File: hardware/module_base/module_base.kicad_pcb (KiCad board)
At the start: 2 copper layers, 100 x 100 mm, 38 parts, among them J1 RJ45_Shielded, J2 Conn_01x24_Female, J3 Conn_01x32_Female, Q1 Q_NMOS_GSD, Q2 Q_NMOS_GSD, Q3 Q_NMOS_GSD, Q4 Q_NMOS_GSD, Q5 Q_NMOS_GSD, Q6 Q_NMOS_GSD, U1 WAVGAT_CAN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

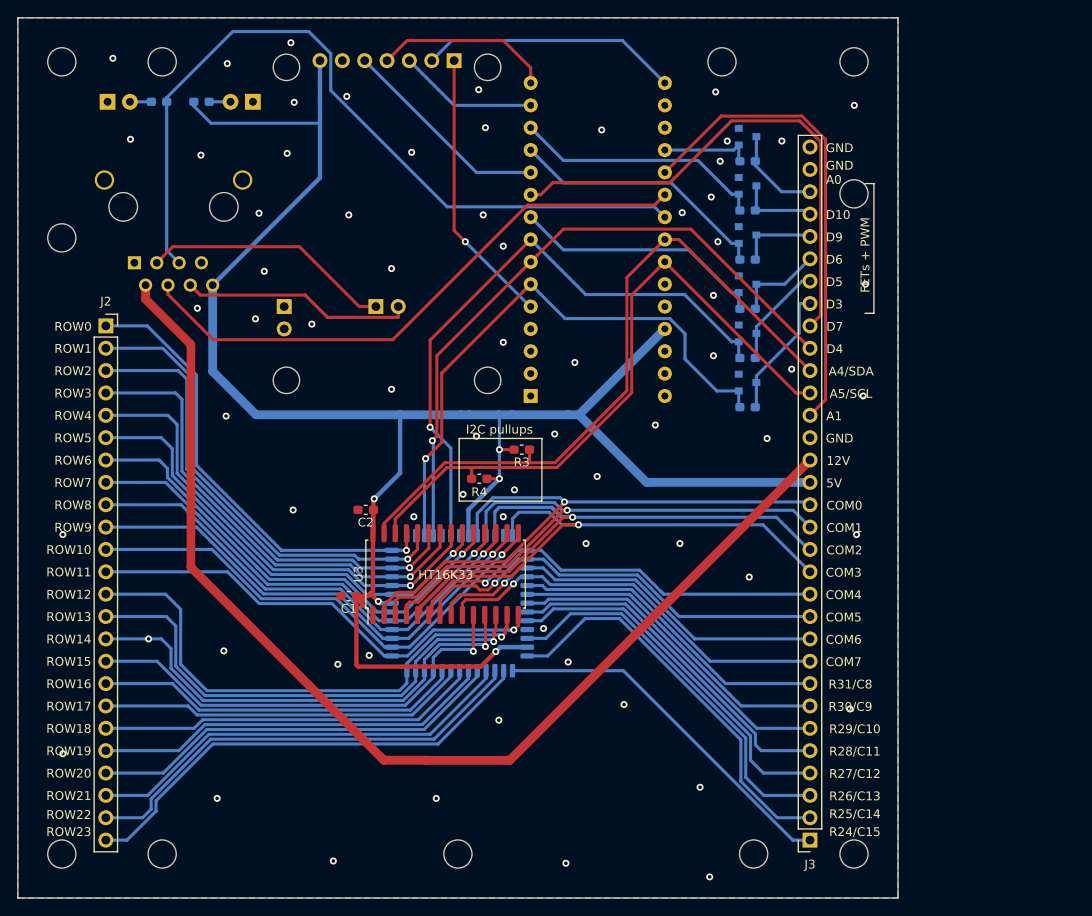
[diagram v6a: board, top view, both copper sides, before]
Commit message: ModuleBase PCB: expose Arduino pins + SPI + more GND/5V
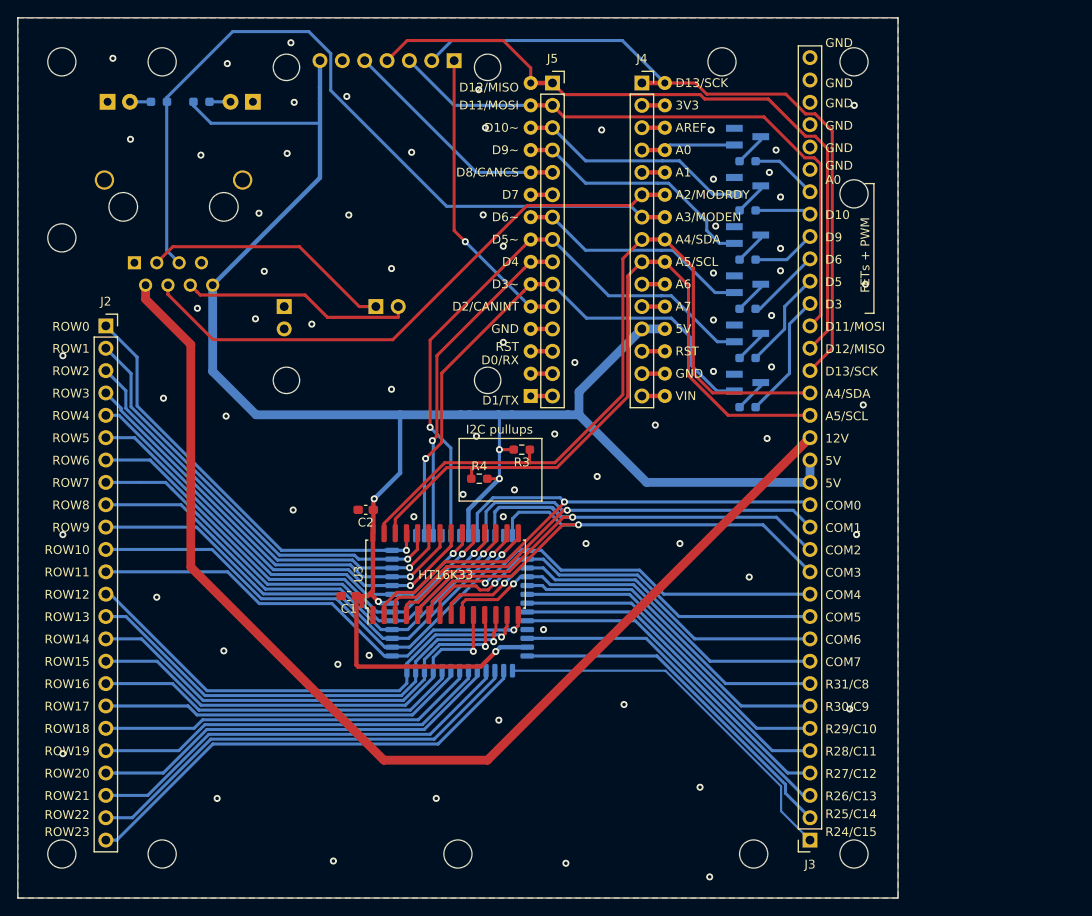
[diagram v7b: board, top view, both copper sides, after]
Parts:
- added J4: Conn_01x15_Female, Connector_PinSocket_2.54mm:PinSocket_1x15_P2.54mm_Vertical, F.Cu at (120.9, 57.4)
- added J5: Conn_01x15_Female, Connector_PinSocket_2.54mm:PinSocket_1x15_P2.54mm_Vertical, F.Cu at (110.7, 57.4)
- C1, C2: footprint Capacitor_SMD:C_0603_1608Metric_Pad1.05x0.95mm_HandSolder -> Capacitor_SMD:C_0603_1608Metric_Pad1.08x0.95mm_HandSolder
- J3: value Conn_01x32_Female -> Conn_01x36_Female; footprint Connector_PinSocket_2.54mm:PinSocket_1x32_P2.54mm_Vertical -> Connector_PinSocket_2.54mm:PinSocket_1x36_P2.54mm_Vertical
- Q1, Q2, Q3, Q4, Q5, Q6: footprint Package_TO_SOT_SMD:SOT-23 -> Package_TO_SOT_SMD:SOT-23_Handsoldering
- R1, R10, R2, R3, R4, R5, R6, R7, R8, R9: footprint Resistor_SMD:R_0603_1608Metric_Pad1.05x0.95mm_HandSolder -> Resistor_SMD:R_0603_1608Metric_Pad0.98x0.95mm_HandSolder
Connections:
- net MODULE_ENABLE renamed A3_MODULE_ENABLE
- net MODULE_READY renamed A2_MODULE_READY
- net Net-(A1-Pad11) renamed D8_CAN_CS
- net Net-(A1-Pad5) renamed D2_CAN_INT
- A1 pad 1: Net-(A1-Pad1) -> D1_TX
- A1 pad 14: MOSI -> D11_MOSI
- A1 pad 15: MISO -> D12_MISO
- A1 pad 16: SCK -> D13_SCK
- A1 pad 17: Net-(A1-Pad17) -> +3V3
- A1 pad 18: Net-(A1-Pad18) -> AREF
- A1 pad 2: Net-(A1-Pad2) -> D0_RX
- A1 pad 28: Net-(A1-Pad28) -> RST
- A1 pad 3: Net-(A1-Pad3) -> RST
- A1 pad 30: Net-(A1-Pad30) -> VIN
- J3 pad 18: +12V -> VCC
- J3 pad 19: GND -> +12V
- J3 pad 20: A1 -> A5_SCL
- J3 pad 21: A5_SCL -> A4_SDA
- J3 pad 22: A4_SDA -> D13_SCK
- J3 pad 23: D4 -> D12_MISO
- J3 pad 24: D7 -> D11_MOSI
- Q1 pad 3: Net-(J3-Pad25) -> Net-(Q1-Pad3)
- Q2 pad 3: Net-(J3-Pad26) -> Net-(Q2-Pad3)
- Q3 pad 3: Net-(J3-Pad27) -> Net-(Q3-Pad3)
- Q4 pad 3: Net-(J3-Pad28) -> Net-(Q4-Pad3)
- Q5 pad 3: Net-(J3-Pad29) -> Net-(Q5-Pad3)
- Q6 pad 3: Net-(J3-Pad30) -> Net-(Q6-Pad3)
- R10 pad 2: A0 -> Net-(Q6-Pad3)
- R5 pad 2: D3 -> Net-(Q1-Pad3)
- R6 pad 2: D5 -> Net-(Q2-Pad3)
- R7 pad 2: D6 -> Net-(Q3-Pad3)
- R8 pad 2: D9 -> Net-(Q4-Pad3)
- R9 pad 2: D10 -> Net-(Q5-Pad3)
- U1 pad J4_2: SCK -> D13_SCK
- U1 pad J4_3: MOSI -> D11_MOSI
- U1 pad J4_4: MISO -> D12_MISO
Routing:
- net D13_SCK: track 0.00 -> 81.6 mm
- net D12_MISO: track 0.00 -> 80.6 mm
- net D11_MOSI: track 0.00 -> 70.5 mm
- net D7: track 58.8 -> 2.47 mm
- net A1: track 54.1 -> 2.61 mm
- net D4: track 74.6 -> 38.2 mm
- net SCK: track 29.4 -> 0.00 mm
- net MISO: track 20.3 -> 0.00 mm
- net MOSI: track 15.9 -> 0.00 mm
- net A4_SDA: track 78.1 -> 87.7 mm
- net A5_SCL: track 74.8 -> 83.4 mm
- net Net-(J3-Pad2): track 46.0 -> 40.3 mm
- net RST: track 0.00 -> 5.08 mm
- net GND: track 0.00 -> 5.08 mm, vias 68 -> 73
- net Net-(J3-Pad3): track 44.5 -> 39.5 mm
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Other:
- board text added: "3V3"
- board text added: "A2/MODRDY"
- board text added: "A3/MODEN"
- board text added: "A6"
- board text added: "A7"
- board text added: "AREF"
- board text added: "D0/RX"
- board text added: "D1/TX"
- board text added: "D10~~"
- board text added: "D11/MOSI"
- board text added: "D12/MISO"
- board text added: "D13/SCK"
- board text added: "D2/CANINT"
- board text added: "D3~~"
- board text added: "D5~~"
- board text added: "D6~~"
- board text added: "D8/CANCS"
- board text added: "D9~~"
- board text added: "FET + resistor in series"
- board text added: "RST"
- board text added: "VIN"
- board text removed: "Choose FET or resistor for each pin"

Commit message: ModuleBase PCB: longer pads for HT1632C footprint
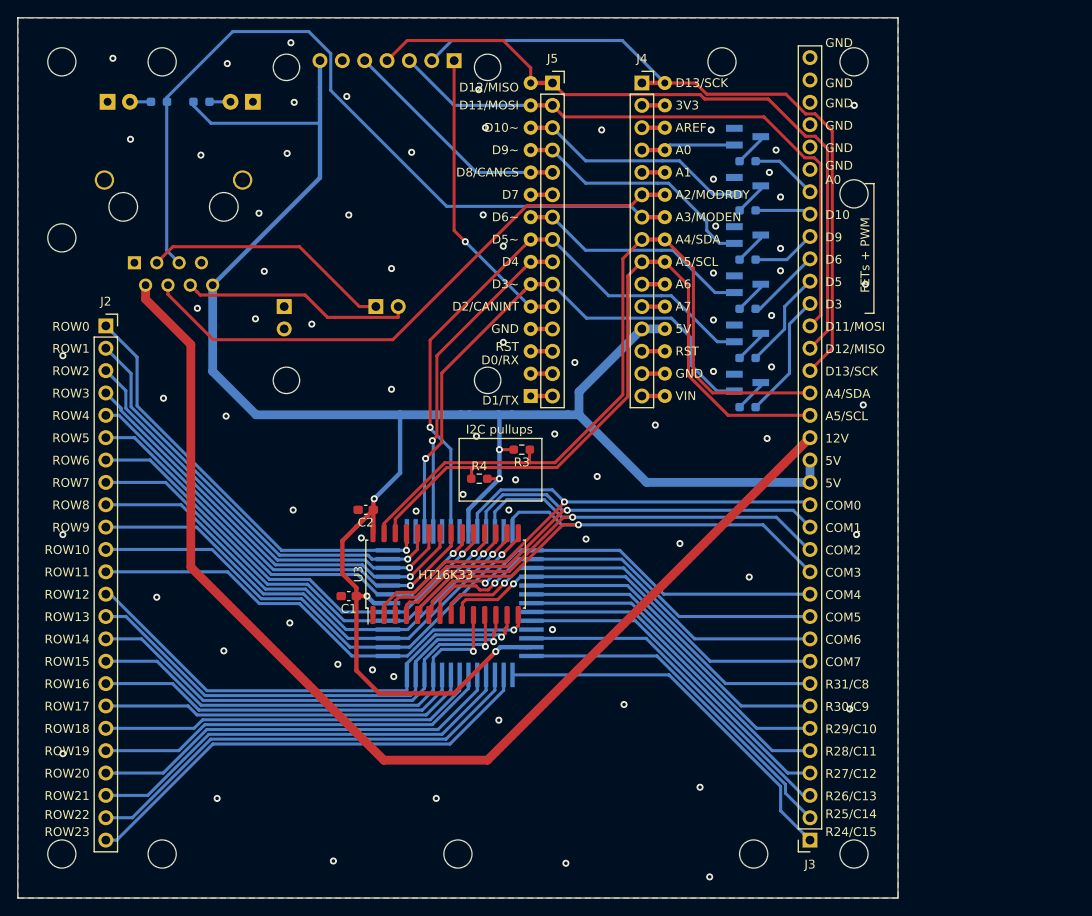
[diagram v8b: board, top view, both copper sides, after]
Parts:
- U2: footprint Package_QFP:LQFP-52_14x14mm_P1mm -> ProjectChips:QFP-52_14x14_Pitch1mm_HandSoldering
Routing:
- net COM2: track 74.3 -> 65.1 mm
- net VCC: track 222.2 -> 227.1 mm
- net ROW5: track 51.5 -> 52.4 mm
- net ROW15: track 52.0 -> 52.9 mm
- net ROW13: track 55.0 -> 55.6 mm
- net ROW14: track 53.7 -> 54.3 mm
- net GND: vias 73 -> 76
